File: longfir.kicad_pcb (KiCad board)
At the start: 2 copper layers, 136.6 x 97.9 mm, 36 parts, among them J1 Haptic, J2 TRRS, K1 diode-choc, K10 diode-choc, K11 diode-choc, K12 diode-choc, K13 diode-choc, K14 diode-choc, K15 diode-choc, K16 diode-choc, K17 diode-choc, K18 diode-choc, K19 diode-choc, K2 diode-choc, K20 diode-choc, K21 diode-choc, K22 diode-choc, K23 diode-choc, K24 diode-choc, K3 diode-choc, K4 diode-choc, K5 diode-choc, K6 diode-choc, K7 diode-choc, K8 diode-choc, K9 diode-choc, SW1 Reset, U1 ProMicro_r

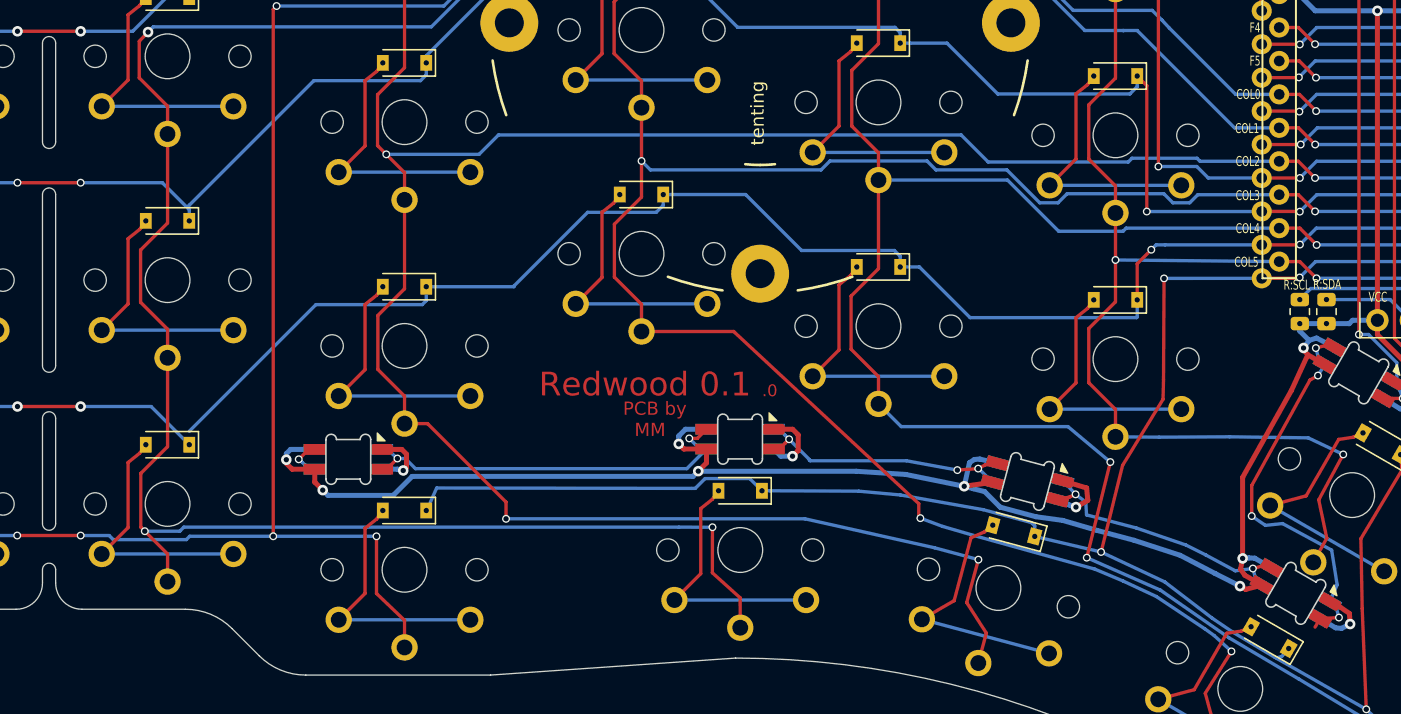
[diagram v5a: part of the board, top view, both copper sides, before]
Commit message: Keepout area for LED top shine experiment
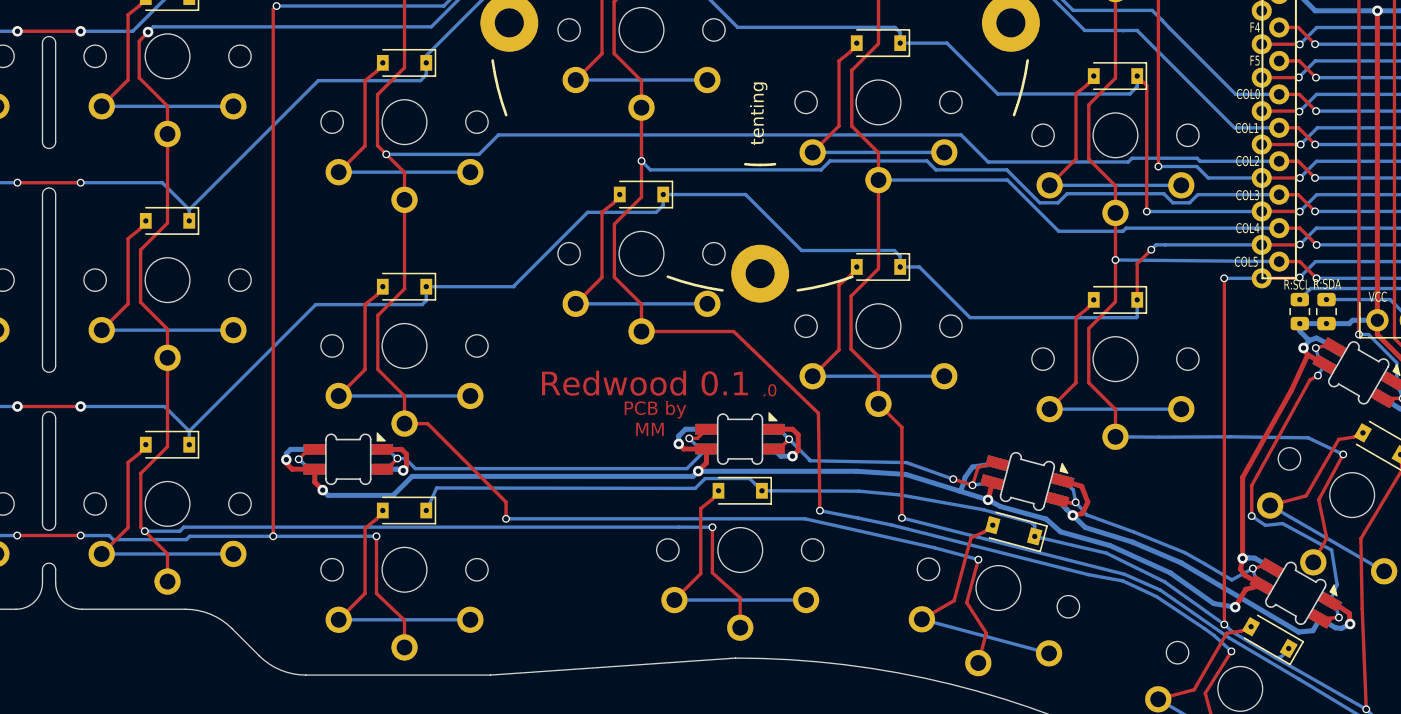
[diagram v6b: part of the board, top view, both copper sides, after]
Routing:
- net GND: track 54.5 -> 76.8 mm
- net col3: track 165.3 -> 168.8 mm
- net col4: track 153.9 -> 150.8 mm, vias 4 -> 3
- net Net-(D3-Pad2): track 21.5 -> 22.7 mm
- net Net-(D1-Pad2): track 30.8 -> 30.0 mm
- net row2: track 137.2 -> 137.8 mm
